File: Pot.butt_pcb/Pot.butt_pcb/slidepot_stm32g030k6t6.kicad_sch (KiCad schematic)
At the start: 6 parts, among them J3 Conn_01x06_Male, SW10 SW_Push, U2 STM32G030K6T6

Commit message: fixing keyboard and pot project schematics
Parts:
- removed J3: Conn_01x06_Male, Connector_PinSocket_2.54mm:PinSocket_1x06_P2.54mm_Horizontal, symbol Connector:Conn_01x06_Male
- added J3: Conn_01x05_Male, symbol Connector:Conn_01x05_Male
- added R20: 100k, Resistor_SMD:R_0805_2012Metric_Pad1.20x1.40mm_HandSolder, symbol Device:R
- C17: value 100nF -> 100n
- C18: value 4.7u -> 100n
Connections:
- net +3V3: now also C18.1, U2.4 (VDD/VDDA), J3.1 (Pin_1), R20.1
- net GND: now also C17.2, C18.2, J3.3 (Pin_3)
- net NRSTs: now also J3.5 (Pin_5), R20.2
- net SWCLKs: now also J3.2 (Pin_2)
- net SWDIOs: now also J3.4 (Pin_4)
- removed net vdds: C18.2, U2.4 (VDD/VDDA)
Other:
- note removed: "SWOp nincs"

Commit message: main_func pcb done
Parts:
- added D55: GREEN LED, LED_SMD:LED_0805_2012Metric_Pad1.15x1.40mm_HandSolder, symbol Device:LED
- added D56: RED LED, LED_SMD:LED_0805_2012Metric_Pad1.15x1.40mm_HandSolder, symbol Device:LED
- added R29, R30: 1k, Resistor_SMD:R_0805_2012Metric_Pad1.20x1.40mm_HandSolder, symbol Device:R
- C17, C18: value 100n -> 100nF
- J3: footprint (none) -> Connector_PinSocket_2.54mm:PinSocket_1x05_P2.54mm_Horizontal
- SW10: footprint (none) -> tactile_button:ROCPU Switches TP10721645
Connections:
- net +3V3: now also D55.2 (A)
- net GND: now also D56.1 (K)
- net USART1_TXs: now also R29.1, R30.1
- new net: D56.2 (A), R30.2
- new net: D55.1 (K), R29.2
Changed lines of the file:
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@@
   (junction (at 162.56 83.82) (diameter 0) (color 0 0 0 0)
   )
+  (junction (at 220.98 102.87) (diameter 0) (color 0 0 0 0)
+  )
   (junction (at 226.06 69.85) (diameter 0) (color 0 0 0 0)
   )
@@
     (stroke (width 0) (type default) (color 0 0 0 0))
   )
+  (wire (pts (xy 198.12 135.89) (xy 203.2 135.89))
+    (stroke (width 0) (type default) (color 0 0 0 0))
+  )
   (wire (pts (xy 165.1 85.09) (xy 165.1 83.82))
     (stroke (width 0) (type default) (color 0 0 0 0))
@@
     (stroke (width 0) (type default) (color 0 0 0 0))
   )
+  (wire (pts (xy 203.2 135.89) (xy 203.2 127))
+    (stroke (width 0) (type default) (color 0 0 0 0))
+  )
   (wire (pts (xy 133.35 58.42) (xy 143.51 58.42))
     (stroke (width 0) (type default) (color 0 0 0 0))
@@
     (stroke (width 0) (type default) (color 0 0 0 0))
   )
+  (wire (pts (xy 198.12 133.35) (xy 198.12 135.89))
+    (stroke (width 0) (type default) (color 0 0 0 0))
+  )
   (wire (pts (xy 237.49 44.45) (xy 237.49 40.64))
     (stroke (width 0) (type default) (color 0 0 0 0))
@@
     (stroke (width 0) (type default) (color 0 0 0 0))
   )
+  (wire (pts (xy 220.98 127) (xy 220.98 134.62))
+    (stroke (width 0) (type default) (color 0 0 0 0))
+  )
   (wire (pts (xy 133.35 63.5) (xy 143.51 63.5))
     (stroke (width 0) (type default) (color 0 0 0 0))
   )
+  (wire (pts (xy 228.6 102.87) (xy 220.98 102.87))
+    (stroke (width 0) (type default) (color 0 0 0 0))
+  )
+  (wire (pts (xy 203.2 102.87) (xy 203.2 106.68))
+    (stroke (width 0) (type default) (color 0 0 0 0))
+  )
   (wire (pts (xy 133.35 60.96) (xy 143.51 60.96))
     (stroke (width 0) (type default) (color 0 0 0 0))
@@
     (stroke (width 0) (type default) (color 0 0 0 0))
   )
+  (wire (pts (xy 220.98 102.87) (xy 220.98 106.68))
+    (stroke (width 0) (type default) (color 0 0 0 0))
+  )
   (wire (pts (xy 49.53 73.66) (xy 57.15 73.66))
     (stroke (width 0) (type default) (color 0 0 0 0))
@@
     (stroke (width 0) (type default) (color 0 0 0 0))
   )
+  (wire (pts (xy 220.98 114.3) (xy 220.98 119.38))
+    (stroke (width 0) (type default) (color 0 0 0 0))
+  )
   (wire (pts (xy 133.35 88.9) (xy 138.43 88.9))
     (stroke (width 0) (type default) (color 0 0 0 0))
   )
+  (wire (pts (xy 203.2 114.3) (xy 203.2 119.38))
+    (stroke (width 0) (type default) (color 0 0 0 0))
+  )
+  (wire (pts (xy 220.98 102.87) (xy 203.2 102.87))
+    (stroke (width 0) (type default) (color 0 0 0 0))
+  )
   (wire (pts (xy 153.67 86.36) (xy 153.67 83.82))
     (stroke (width 0) (type default) (color 0 0 0 0))
@@
     (effects (font (size 1.27 1.27)) (justify left))
     (property "Intersheet References" "${INTERSHEET_REFS}" (id 0) (at 153.7245 73.5806 0)
+      (effects (font (size 1.27 1.27)) (justify left) hide)
+    )
+  )
+  (global_label "USART1_TXs" (shape input) (at 228.6 102.87 0) (fields_autoplaced)
+    (effects (font (size 1.27 1.27)) (justify left))
+    (property "Intersheet References" "${INTERSHEET_REFS}" (id 0) (at 242.2617 102.7906 0)
       (effects (font (size 1.27 1.27)) (justify left) hide)
     )
@@
     (pin "1")
   )
+  (symbol (lib_id "power:+3.3V") (at 198.12 133.35 0) (unit 1)
+    (in_bom yes) (on_board yes) (fields_autoplaced)
+    (property "Reference" "#PWR024" (id 0) (at 198.12 137.16 0)
+      (effects (font (size 1.27 1.27)) hide)
+    )
+    (property "Value" "+3.3V" (id 1) (at 198.12 128.27 0))
+    (property "Footprint" "" (id 2) (at 198.12 133.35 0)
+      (effects (font (size 1.27 1.27)) hide)
+    )
+    (property "Datasheet" "" (id 3) (at 198.12 133.35 0)
+      (effects (font (size 1.27 1.27)) hide)
+    )
+    (pin "1")
+  )
+  (symbol (lib_id "Device:LED") (at 220.98 123.19 90) (unit 1)
+    (in_bom yes) (on_board yes) (fields_autoplaced)
+    (property "Reference" "D56" (id 0) (at 224.79 123.5074 90)
+      (effects (font (size 1.27 1.27)) (justify right))
+    )
+    (property "Value" "RED LED" (id 1) (at 224.79 126.0474 90)
+      (effects (font (size 1.27 1.27)) (justify right))
+    )
+    (property "Footprint" "LED_SMD:LED_0805_2012Metric_Pad1.15x1.40mm_HandSolder" (id 2) (at 220.98 123.19 0)
+      (effects (font (size 1.27 1.27)) hide)
+    )
+    (property "Datasheet" "~" (id 3) (at 220.98 123.19 0)
+      (effects (font (size 1.27 1.27)) hide)
+    )
+    (pin "1")
+    (pin "2")
+  )
+  (symbol (lib_id "Device:R") (at 220.98 110.49 0) (unit 1)
+    (in_bom yes) (on_board yes) (fields_autoplaced)
+    (property "Reference" "R30" (id 0) (at 223.52 109.2199 0)
+      (effects (font (size 1.27 1.27)) (justify left))
+    )
+    (property "Value" "1k" (id 1) (at 223.52 111.7599 0)
+      (effects (font (size 1.27 1.27)) (justify left))
+    )
+    (property "Footprint" "Resistor_SMD:R_0805_2012Metric_Pad1.20x1.40mm_HandSolder" (id 2) (at 219.202 110.49 90)
+      (effects (font (size 1.27 1.27)) hide)
+    )
+    (property "Datasheet" "~" (id 3) (at 220.98 110.49 0)
+      (effects (font (size 1.27 1.27)) hide)
+    )
+    (pin "1")
+    (pin "2")
+  )
   (symbol (lib_id "power:+3.3V") (at 162.56 67.31 0) (unit 1)
     (in_bom yes) (on_board yes) (fields_autoplaced)
@@
     (property "Reference" "J3" (id 0) (at 224.155 39.37 0))
     (property "Value" "Conn_01x05_Male" (id 1) (at 224.155 41.91 0))
-    (property "Footprint" "" (id 2) (at 223.52 49.53 0)
+    (property "Footprint" "Connector_PinSocket_2.54mm:PinSocket_1x05_P2.54mm_Horizontal" (id 2) (at 223.52 49.53 0)
       (effects (font (size 1.27 1.27)) hide)
     )
@@
     (pin "5")
   )
+  (symbol (lib_id "power:GND") (at 220.98 134.62 0) (unit 1)
+    (in_bom yes) (on_board yes) (fields_autoplaced)
+    (property "Reference" "#PWR025" (id 0) (at 220.98 140.97 0)
+      (effects (font (size 1.27 1.27)) hide)
+    )
+    (property "Value" "GND" (id 1) (at 220.98 139.7 0))
+    (property "Footprint" "" (id 2) (at 220.98 134.62 0)
+      (effects (font (size 1.27 1.27)) hide)
+    )
+    (property "Datasheet" "" (id 3) (at 220.98 134.62 0)
+      (effects (font (size 1.27 1.27)) hide)
+    )
+    (pin "1")
+  )
+  (symbol (lib_id "Device:R") (at 203.2 110.49 0) (unit 1)
+    (in_bom yes) (on_board yes) (fields_autoplaced)
+    (property "Reference" "R29" (id 0) (at 205.74 109.2199 0)
+      (effects (font (size 1.27 1.27)) (justify left))
+    )
+    (property "Value" "1k" (id 1) (at 205.74 111.7599 0)
+      (effects (font (size 1.27 1.27)) (justify left))
+    )
+    (property "Footprint" "Resistor_SMD:R_0805_2012Metric_Pad1.20x1.40mm_HandSolder" (id 2) (at 201.422 110.49 90)
+      (effects (font (size 1.27 1.27)) hide)
+    )
+    (property "Datasheet" "~" (id 3) (at 203.2 110.49 0)
+      (effects (font (size 1.27 1.27)) hide)
+    )
+    (pin "1")
+    (pin "2")
+  )
   (symbol (lib_id "Device:C") (at 226.06 73.66 0) (unit 1)
     (in_bom yes) (on_board yes) (fields_autoplaced)
@@
       (effects (font (size 1.27 1.27)) (justify left))
     )
-    (property "Value" "100n" (id 1) (at 229.87 74.9299 0)
+    (property "Value" "100nF" (id 1) (at 229.87 74.9299 0)
       (effects (font (size 1.27 1.27)) (justify left))
     )
@@
       (effects (font (size 1.27 1.27)) (justify left))
     )
-    (property "Footprint" "" (id 2) (at 170.18 90.17 0)
+    (property "Footprint" "tactile_button:ROCPU Switches TP10721645" (id 2) (at 170.18 90.17 0)
       (effects (font (size 1.27 1.27)) hide)
     )
@@
     (pin "1")
   )
+  (symbol (lib_id "Device:LED") (at 203.2 123.19 270) (unit 1)
+    (in_bom yes) (on_board yes) (fields_autoplaced)
+    (property "Reference" "D55" (id 0) (at 205.74 120.3324 90)
+      (effects (font (size 1.27 1.27)) (justify left))
+    )
+    (property "Value" "GREEN LED" (id 1) (at 205.74 122.8724 90)
+      (effects (font (size 1.27 1.27)) (justify left))
+    )
+    (property "Footprint" "LED_SMD:LED_0805_2012Metric_Pad1.15x1.40mm_HandSolder" (id 2) (at 203.2 123.19 0)
+      (effects (font (size 1.27 1.27)) hide)
+    )
+    (property "Datasheet" "~" (id 3) (at 203.2 123.19 0)
+      (effects (font (size 1.27 1.27)) hide)
+    )
+    (pin "1")
+    (pin "2")
+  )
   (symbol (lib_id "Device:R") (at 162.56 73.66 0) (unit 1)
     (in_bom yes) (on_board yes) (fields_autoplaced)
@@
       (effects (font (size 1.27 1.27)) (justify left))
     )
-    (property "Value" "100n" (id 1) (at 241.3 74.9299 0)
-      (effects (font (size 1.27 1.27)) (justify left))
-    )
+    (property "Value" "100nF" (id 1) (at 241.3 74.9299 0)
+      (effects (font (size 1.27 1.27)) (justify left))
+    )

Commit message: Pot.but_pcb in progress
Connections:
- net 1st_Row: now also U2.26 (PA15); no longer U2.18 (PA8)
- net 2nd_Row: now also U2.23 (PA12); no longer U2.22 (PA11)
- net 3rd_Row: now also U2.22 (PA11); no longer U2.23 (PA12)
- net 4th_Row: now also U2.20 (PC6); no longer U2.26 (PA15)
- net 5th_Row: now also U2.18 (PA8); no longer U2.20 (PC6)
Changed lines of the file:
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@@
     )
   )
-  (global_label "4th_Row" (shape input) (at 49.53 83.82 180) (fields_autoplaced)
+  (global_label "1st_Row" (shape input) (at 49.53 83.82 180) (fields_autoplaced)
     (effects (font (size 1.27 1.27)) (justify right))
-    (property "Intersheet References" "${INTERSHEET_REFS}" (id 0) (at 39.3155 83.7406 0)
+    (property "Intersheet References" "${INTERSHEET_REFS}" (id 0) (at 39.4364 83.7406 0)
       (effects (font (size 1.27 1.27)) (justify right) hide)
     )
@@
     )
   )
-  (global_label "2nd_Row" (shape input) (at 49.53 73.66 180) (fields_autoplaced)
+  (global_label "3rd_Row" (shape input) (at 49.53 73.66 180) (fields_autoplaced)
     (effects (font (size 1.27 1.27)) (justify right))
-    (property "Intersheet References" "${INTERSHEET_REFS}" (id 0) (at 38.8921 73.5806 0)
+    (property "Intersheet References" "${INTERSHEET_REFS}" (id 0) (at 39.255 73.5806 0)
       (effects (font (size 1.27 1.27)) (justify right) hide)
     )
@@
     )
   )
-  (global_label "1st_Row" (shape input) (at 49.53 66.04 180) (fields_autoplaced)
+  (global_label "5th_Row" (shape input) (at 49.53 66.04 180) (fields_autoplaced)
     (effects (font (size 1.27 1.27)) (justify right))
-    (property "Intersheet References" "${INTERSHEET_REFS}" (id 0) (at 39.4364 65.9606 0)
+    (property "Intersheet References" "${INTERSHEET_REFS}" (id 0) (at 39.3155 65.9606 0)
       (effects (font (size 1.27 1.27)) (justify right) hide)
     )
@@
     )
   )
-  (global_label "5th_Row" (shape input) (at 143.51 73.66 0) (fields_autoplaced)
+  (global_label "4th_Row" (shape input) (at 143.51 73.66 0) (fields_autoplaced)
     (effects (font (size 1.27 1.27)) (justify left))
     (property "Intersheet References" "${INTERSHEET_REFS}" (id 0) (at 153.7245 73.5806 0)
@@
     )
   )
-  (global_label "3rd_Row" (shape input) (at 49.53 76.2 180) (fields_autoplaced)
+  (global_label "2nd_Row" (shape input) (at 49.53 76.2 180) (fields_autoplaced)
     (effects (font (size 1.27 1.27)) (justify right))
-    (property "Intersheet References" "${INTERSHEET_REFS}" (id 0) (at 39.255 76.1206 0)
+    (property "Intersheet References" "${INTERSHEET_REFS}" (id 0) (at 38.8921 76.1206 0)
       (effects (font (size 1.27 1.27)) (justify right) hide)
     )

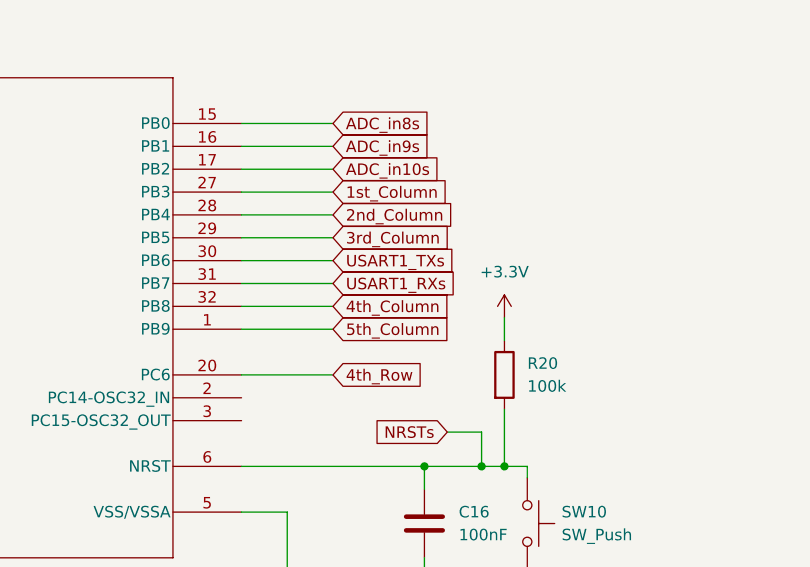
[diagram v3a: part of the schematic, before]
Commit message: Pot.butt_pcb done
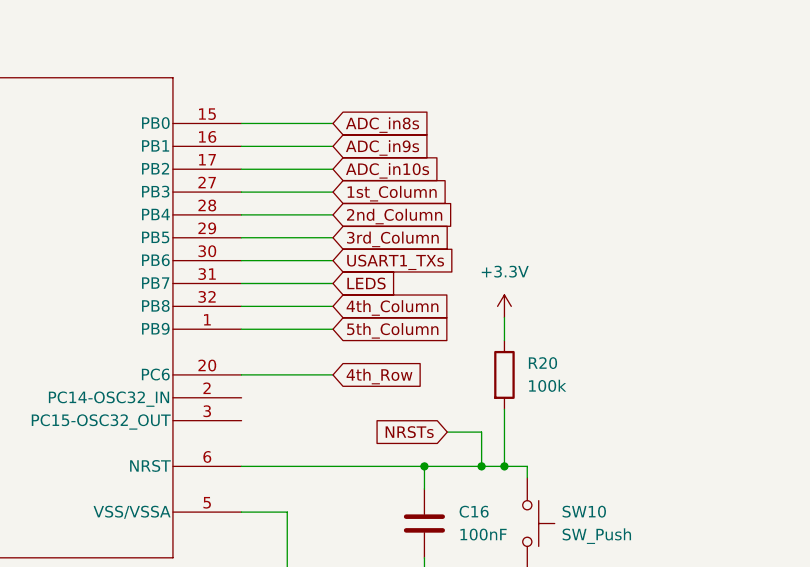
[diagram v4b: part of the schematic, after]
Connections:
- net USART1_RXs renamed LEDS
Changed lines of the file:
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@@
     )
   )
-  (global_label "USART1_RXs" (shape input) (at 143.51 63.5 0) (fields_autoplaced)
+  (global_label "LEDS" (shape input) (at 143.51 63.5 0) (fields_autoplaced)
     (effects (font (size 1.27 1.27)) (justify left))
-    (property "Intersheet References" "${INTERSHEET_REFS}" (id 0) (at 157.4741 63.5794 0)
+    (property "Intersheet References" "${INTERSHEET_REFS}" (id 0) (at 150.5798 63.4206 0)
       (effects (font (size 1.27 1.27)) (justify left) hide)
     )

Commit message: pcb design fixing
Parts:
- removed C18: 100nF, Capacitor_SMD:C_0805_2012Metric_Pad1.18x1.45mm_HandSolder, symbol Device:C
- removed D56: RED LED, LED_SMD:LED_0805_2012Metric_Pad1.15x1.40mm_HandSolder, symbol Device:LED
- removed R29, R30: 1k, Resistor_SMD:R_0805_2012Metric_Pad1.20x1.40mm_HandSolder, symbol Device:R
- added R3: 1k, Resistor_SMD:R_0805_2012Metric_Pad1.20x1.40mm_HandSolder, symbol Device:R
- D55: value GREEN LED -> RED LED
- R20: value 100k -> 10k
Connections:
- net +3V3: no longer D55.2 (A)
- net GND: now also D55.1 (K)
- net STATUS_LEDs: now reaches U2.3 (PC15-OSC32_OUT)
- net STATUS_LEDs: now also R3.1
- net ADC_in10s: no longer names the net of U2.17 (PB2)
- net ADC_in8s: no longer names the net of U2.15 (PB0)
- net ADC_in9s: no longer names the net of U2.16 (PB1)
- net USART1_TXs: no longer names the net of U2.30 (PB6)
- new net: D55.2 (A), R3.2
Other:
- moved on the sheet: C17
